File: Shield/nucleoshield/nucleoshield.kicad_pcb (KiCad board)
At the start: 2 copper layers, 99.6 x 99.6 mm, 2 parts, among them J1 Conn_02x19_Odd_Even, J2 Conn_02x19_Odd_Even

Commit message: Schematic and pcb ready
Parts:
- added C1: 470u, Capacitor_THT:CP_Radial_D8.0mm_P3.50mm, F.Cu at (98.3, 121.7)
- added C2: 47u, Capacitor_SMD:C_1206_3216Metric, F.Cu at (74.5, 126.7)
- added C3: 100n, Capacitor_SMD:C_1206_3216Metric, F.Cu at (95.6, 97.6)
- added C4: 100n, Capacitor_SMD:C_1206_3216Metric, F.Cu at (100.0, 114.4)
- added C5: 470u, Capacitor_THT:CP_Radial_D8.0mm_P3.50mm, F.Cu at (86.4, 95.8)
- added C6: 10u, Capacitor_SMD:C_1206_3216Metric, F.Cu at (102.9, 56.5)
- added C7: 100n, Capacitor_SMD:C_1206_3216Metric, F.Cu at (116.0, 46.5)
- added D1: LED, LED_SMD:LED_0805_2012Metric, F.Cu at (75.4, 62.8)
- added IC1: L80-M39, componentLib:L80-M39, F.Cu at (81.7, 51.4)
- added J10: ENCODER_3, Connector_PinSocket_2.54mm:PinSocket_1x04_P2.54mm_Vertical, F.Cu at (147.4, 107.7)
- added J11: MPU9250, Connector_PinHeader_2.54mm:PinHeader_1x10_P2.54mm_Vertical, F.Cu at (109.2, 45.1)
- added J3: POWER, Connector_PinHeader_2.54mm:PinHeader_1x03_P2.54mm_Vertical, F.Cu at (86.7, 130.7)
- added J4: MOTOR_1, Connector_PinSocket_2.54mm:PinSocket_1x04_P2.54mm_Vertical, F.Cu at (60.6, 94.2)
- added J5: ENCODER_1, Connector_PinSocket_2.54mm:PinSocket_1x04_P2.54mm_Vertical, F.Cu at (60.6, 107.7)
- added J6: ENCODER_2, Connector_PinSocket_2.54mm:PinSocket_1x04_P2.54mm_Vertical, F.Cu at (113.5, 130.6)
- added J7: MOTOR_2, Connector_PinSocket_2.54mm:PinSocket_1x04_P2.54mm_Vertical, F.Cu at (98.8, 130.6)
- added J8: LCD_I2C, Connector_PinSocket_2.54mm:PinSocket_1x04_P2.54mm_Vertical, F.Cu at (146.7, 53.4)
- added J9: MOTOR_3, Connector_PinSocket_2.54mm:PinSocket_1x04_P2.54mm_Vertical, F.Cu at (147.4, 94.2)
- added JP1: AVDD-3.3V, Jumper:SolderJumper-2_P1.3mm_Bridged2Bar_Pad1.0x1.5mm, F.Cu at (146.9, 82.7)
- added Q1: BSS138, Package_TO_SOT_SMD:SOT-23, F.Cu at (136.4, 55.3)
- added Q2: BSS138, Package_TO_SOT_SMD:SOT-23, F.Cu at (136.4, 61.2)
- added R1: 10k, Resistor_SMD:R_0805_2012Metric, F.Cu at (79.2, 119.6)
- added R2: 2k, Resistor_SMD:R_0805_2012Metric, F.Cu at (79.2, 127.0)
- added R3: 2K, Resistor_SMD:R_0805_2012Metric, F.Cu at (131.0, 55.3)
- added R4: 2K, Resistor_SMD:R_0805_2012Metric, F.Cu at (130.9, 61.2)
- added R5: 2K, Resistor_SMD:R_0805_2012Metric, F.Cu at (141.6, 53.9)
- added R6: 2K, Resistor_SMD:R_0805_2012Metric, F.Cu at (143.0, 61.1)
- added R7: 1K, Resistor_SMD:R_0805_2012Metric, F.Cu at (70.9, 61.9)
- added TP1: AVDD, TestPoint:TestPoint_THTPad_1.0x1.0mm_Drill0.5mm, F.Cu at (146.2, 78.1)
- moved J2 33.2 mm to (133.0, 74.8)
- moved J1 33.1 mm to (72.0, 74.8)
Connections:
- J1 pad 1: unconnected-(J1-Pad1) -> GPS_UART_RX
- J1 pad 12: unconnected-(J1-Pad12) -> IOREF
- J1 pad 14: unconnected-(J1-Pad14) -> RESET
- J1 pad 16: unconnected-(J1-Pad16) -> ENCODER_VCC
- J1 pad 18: unconnected-(J1-Pad18) -> LOGIC_5V
- J1 pad 19: unconnected-(J1-Pad19) -> ENCODER_GND
- J1 pad 2: unconnected-(J1-Pad2) -> GPS_UART_TX
- J1 pad 20: unconnected-(J1-Pad20) -> ENCODER_GND
- J1 pad 22: unconnected-(J1-Pad22) -> ENCODER_GND
- J1 pad 23: unconnected-(J1-Pad23) -> ENCODER_A1
- J1 pad 24: unconnected-(J1-Pad24) -> VIN
- J1 pad 25: unconnected-(J1-Pad25) -> ENCODER_B1
- J1 pad 27: unconnected-(J1-Pad27) -> ENCODER_A2
- J1 pad 29: unconnected-(J1-Pad29) -> ENCODER_B2
- J1 pad 3: unconnected-(J1-Pad3) -> GPS_RESET
- J1 pad 31: unconnected-(J1-Pad31) -> ENCODER_A3
- J1 pad 33: unconnected-(J1-Pad33) -> VBAT
- J1 pad 35: unconnected-(J1-Pad35) -> ENCODER_B3
- J1 pad 38: unconnected-(J1-Pad38) -> BAT_ADC
- J1 pad 5: unconnected-(J1-Pad5) -> VDD
- J1 pad 6: unconnected-(J1-Pad6) -> E5V
- J1 pad 8: unconnected-(J1-Pad8) -> ENCODER_GND
- J2 pad 17: unconnected-(J2-Pad17) -> SCL
- J2 pad 19: unconnected-(J2-Pad19) -> SDA
- J2 pad 20: unconnected-(J2-Pad20) -> ENCODER_GND
- J2 pad 21: unconnected-(J2-Pad21) -> INB1
- J2 pad 23: unconnected-(J2-Pad23) -> INA1
- J2 pad 25: unconnected-(J2-Pad25) -> SCL2
- J2 pad 29: unconnected-(J2-Pad29) -> INB3
- J2 pad 3: unconnected-(J2-Pad3) -> INA2
- J2 pad 31: unconnected-(J2-Pad31) -> SDA2
- J2 pad 4: unconnected-(J2-Pad4) -> INA3
- J2 pad 5: unconnected-(J2-Pad5) -> INB2
- J2 pad 7: unconnected-(J2-Pad7) -> AVDD
- J2 pad 8: unconnected-(J2-Pad8) -> U5V
- J2 pad 9: unconnected-(J2-Pad9) -> ENCODER_GND
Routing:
- net ENCODER_VCC: track 0.00 -> 363.9 mm
- net LOGIC_5V: track 0.00 -> 95.7 mm
- net ENCODER_A3: track 0.00 -> 85.7 mm, vias 0 -> 2
- net ENCODER_B3: track 0.00 -> 84.7 mm, vias 0 -> 2
- net ENCODER_B2: track 0.00 -> 80.4 mm, vias 0 -> 1
- net ENCODER_A2: track 0.00 -> 76.7 mm
- net INA1: track 0.00 -> 75.2 mm, vias 0 -> 2
- net INB1: track 0.00 -> 73.0 mm, vias 0 -> 2
- net INA2: track 0.00 -> 69.2 mm
- net INB2: track 0.00 -> 66.1 mm
- net SDA2: track 0.00 -> 66.1 mm, vias 0 -> 3
- net SCL: track 0.00 -> 64.1 mm
- net SDA: track 0.00 -> 63.6 mm
- net E5V: track 0.00 -> 63.0 mm
- net SCL2: track 0.00 -> 49.9 mm, vias 0 -> 2
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- added copper zone on B.Cu, net ENCODER_GND
- added copper zone on F.Cu, net ENCODER_GND
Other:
- board text added: "3V3"
- board text added: "5V"
- board text added: "AD0"
- board text added: "BAT"
- board text added: "ECL"
- board text added: "EDA"
- board text added: "ENA"
- board text added: "ENB"
- board text added: "FSYNC"
- board text added: "GND"
- board text added: "INA"
- board text added: "INB"
- board text added: "INT"
- board text added: "NCS"
- board text added: "SCL"
- board text added: "SDA"

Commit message: power modifications
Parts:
- added JP2: Jumper_3_Open, Connector_PinSocket_2.54mm:PinSocket_1x03_P2.54mm_Vertical, F.Cu at (82.8, 89.1)
- J10, J4, J5, J6, J7, J8, J9: footprint Connector_PinSocket_2.54mm:PinSocket_1x04_P2.54mm_Vertical -> Connector_JST:JST_EH_B4B-EH-A_1x04_P2.50mm_Vertical
- moved R6 1.79 mm to (141.2, 61.2), turned to 180 degrees
- moved J10 0.30 mm to (147.4, 108.0), turned to -90 degrees
- moved J9 0.15 mm to (147.4, 94.3), turned to -90 degrees
- turned J4 to -90 degrees
- turned J5 to -90 degrees
- turned J6 to 0 degrees
- turned J7 to 0 degrees
- turned J8 to -90 degrees
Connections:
- J1 pad 18: LOGIC_5V -> NUCLEO_5V
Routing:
- net NUCLEO_5V: track 0.00 -> 10.8 mm
- net E5V: track 63.0 -> 67.3 mm
- net Net-(J8-Pad4): track 12.3 -> 10.6 mm
- net LOGIC_5V: track 95.7 -> 95.0 mm
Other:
- board text added: "DCDC_5V"
- board text added: "NUC_5V"

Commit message: Power connector
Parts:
- added J12: Screw_Terminal_01x02, TerminalBlock:TerminalBlock_Altech_AK300-2_P5.00mm, F.Cu at (71.9, 43.7)
- added J13: Screw_Terminal_01x02, TerminalBlock:TerminalBlock_Altech_AK300-2_P5.00mm, F.Cu at (58.2, 43.2)
- added JP3: Jumper_3_Open, Connector_PinSocket_2.54mm:PinSocket_1x03_P2.54mm_Vertical, F.Cu at (79.7, 89.9)
- moved JP1 25.5 mm to (121.9, 87.9), turned to -90 degrees
- moved TP1 20.8 mm to (126.0, 82.8)
- moved JP2 12.2 mm to (95.0, 88.9)
- moved C5 7.58 mm to (94.0, 95.9)
- moved C3 4.98 mm to (100.6, 97.6)
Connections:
- net E5V renamed 5V_DCDC
- J1 pad 16: ENCODER_VCC -> NUCLEO_3V3
- JP1 pad 2: ENCODER_VCC -> NUCLEO_3V3
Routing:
- net NUCLEO_3V3: track 0.00 -> 83.5 mm, vias 0 -> 2
- net 5V_DCDC: track 67.3 -> 135.7 mm
- net 3V3_DCDC: track 0.00 -> 48.5 mm
- net ENCODER_VCC: track 363.9 -> 348.8 mm
- net NUCLEO_5V: track 10.8 -> 23.1 mm, vias 0 -> 1
- net LOGIC_5V: track 95.0 -> 84.5 mm
- net AVDD: track 19.0 -> 13.3 mm

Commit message: small changes
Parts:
- JP2, JP3: footprint Connector_PinSocket_2.54mm:PinSocket_1x03_P2.54mm_Vertical -> Connector_PinHeader_2.54mm:PinHeader_1x03_P2.54mm_Vertical
- moved D1 29.2 mm to (94.5, 40.6), turned to -90 degrees
- moved R7 29.2 mm to (94.5, 44.7), turned to -90 degrees
- moved C7 18.8 mm to (100.1, 56.4)
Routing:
- net Net-(IC1-Pad6): track 36.4 -> 5.67 mm
- net Net-(D1-Pad2): track 3.57 -> 2.21 mm

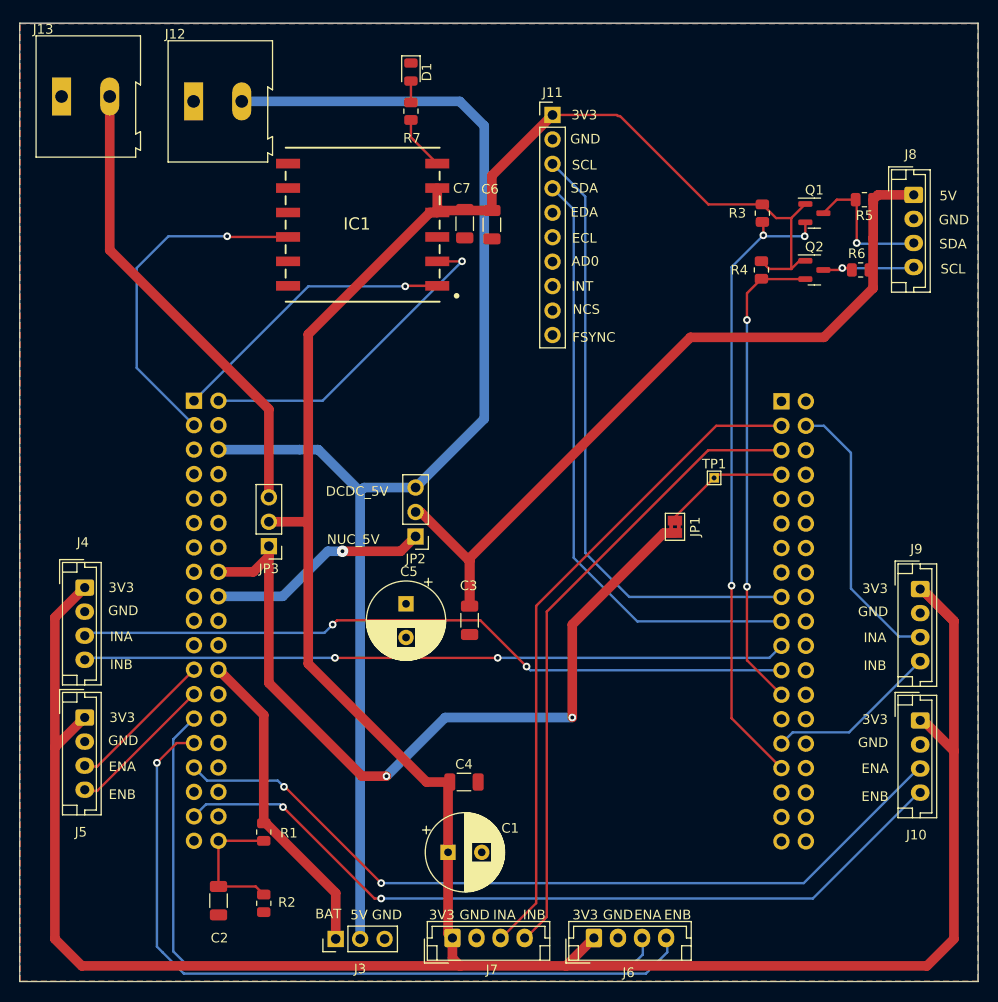
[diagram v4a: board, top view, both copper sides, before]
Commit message: Csatlakozók megváltoztatva, polaritásvédelem, apróbb javítások
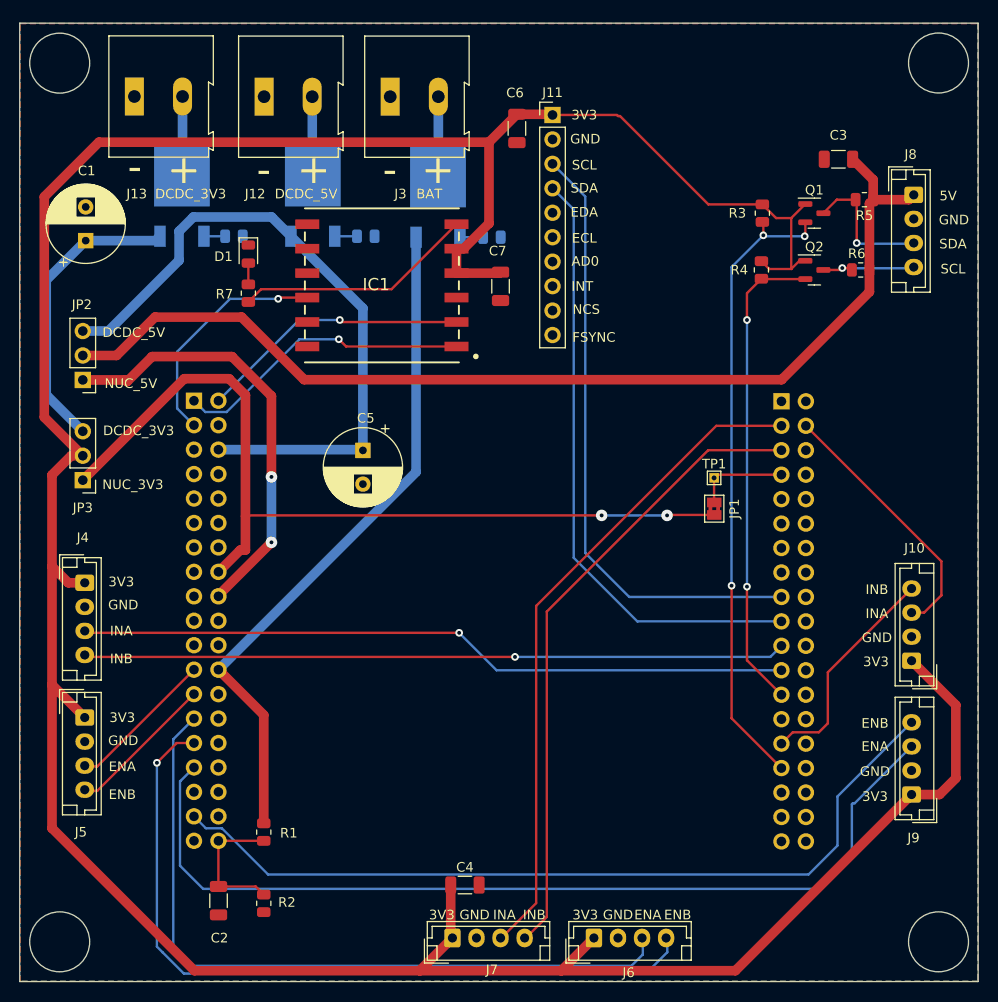
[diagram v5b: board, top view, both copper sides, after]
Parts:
- added Q3: AOD409, Package_TO_SOT_SMD:TO-252-2, B.Cu at (84.3, 53.5)
- added Q4: AOD409, Package_TO_SOT_SMD:TO-252-2, B.Cu at (70.7, 53.5)
- added Q5: AOD409, Package_TO_SOT_SMD:TO-252-2, B.Cu at (97.3, 53.6)
- added R10: 10k, Resistor_SMD:R_0805_2012Metric, B.Cu at (102.9, 57.8)
- added R8: 10k, Resistor_SMD:R_0805_2012Metric, B.Cu at (89.8, 57.7)
- added R9: 10k, Resistor_SMD:R_0805_2012Metric, B.Cu at (76.1, 57.7)
- C2: value 47u -> 22u
- J12: value Screw_Terminal_01x02 -> 5V_DCDC
- J13: value Screw_Terminal_01x02 -> 3V3_DCDC
- J3: value POWER -> Battery; footprint Connector_PinHeader_2.54mm:PinHeader_1x03_P2.54mm_Vertical -> TerminalBlock:TerminalBlock_Altech_AK300-2_P5.00mm
- moved J3 87.7 mm to (92.3, 43.2), turned to 0 degrees
- moved C1 73.9 mm to (60.7, 58.2), turned to 90 degrees
- moved C3 61.3 mm to (138.9, 49.7), turned to 180 degrees
- moved JP2 38.2 mm to (60.4, 72.6)
- moved D1 25.4 mm to (77.6, 59.5)
- moved R7 25.4 mm to (77.6, 63.6)
- moved JP3 20.5 mm to (60.4, 83.0)
- moved C5 16.6 mm to (89.5, 79.9)
- moved C4 10.7 mm to (100.1, 125.1)
- moved C6 10.3 mm to (105.5, 46.5)
- moved J10 7.75 mm to (146.5, 115.7), turned to 90 degrees
- moved J13 7.57 mm to (65.8, 43.2)
- moved J9 7.50 mm to (146.5, 101.8), turned to 90 degrees
- moved C7 7.50 mm to (103.8, 62.9)
- moved J12 7.34 mm to (79.2, 43.2)
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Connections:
- C1 pad 1: ENCODER_VCC -> 3V3_DCDC
- C5 pad 1: LOGIC_5V -> 5V_DCDC
- J12 pad 2: 5V_DCDC -> Net-(J12-Pad2)
- J13 pad 2: 3V3_DCDC -> Net-(J13-Pad2)
- J3 pad 1: VIN -> ENCODER_GND
- J3 pad 2: 5V_DCDC -> Net-(J3-Pad2)
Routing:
- net 5V_DCDC: track 135.7 -> 69.5 mm
- net VIN: track 33.2 -> 71.3 mm
- net LOGIC_5V: track 84.5 -> 109.1 mm
- net NUCLEO_5V: track 23.1 -> 45.5 mm, vias 1 -> 2
- net Net-(IC1-Pad6): track 5.67 -> 25.0 mm
- net 3V3_DCDC: track 48.5 -> 31.0 mm
- net ENCODER_VCC: track 348.9 -> 334.0 mm
- net GPS_RESET: track 35.9 -> 24.2 mm
- net ENCODER_A3: track 85.7 -> 96.8 mm, vias 2 -> 0
- net Net-(J3-Pad2): track 0.00 -> 8.31 mm
- net Net-(J13-Pad2): track 0.00 -> 8.24 mm
- net Net-(J12-Pad2): track 0.00 -> 8.23 mm
- net NUCLEO_3V3: track 83.5 -> 90.6 mm
- net GPS_UART_TX: track 33.9 -> 28.3 mm
- net INB3: track 18.0 -> 23.3 mm
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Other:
- outline, holes or cut-outs redrawn
- board text added: "+"
- board text added: "-"
- board text added: "DCDC_3V3"
- board text added: "NUC_3V3"

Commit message: Fetek kicserélve
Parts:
- Q3, Q4, Q5: value AOD409 -> AO3401A; footprint Package_TO_SOT_SMD:TO-252-2 -> Package_TO_SOT_SMD:SOT-23
- moved R8 4.04 mm to (89.2, 53.7)
- moved R10 3.98 mm to (102.1, 53.9)
- moved R9 2.73 mm to (75.0, 55.2)
- moved Q3 0.81 mm to (84.2, 52.7)
- moved Q4 0.80 mm to (70.7, 52.7)
- moved Q5 0.50 mm to (97.3, 53.1)
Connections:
- Q3 pad 2: Net-(J12-Pad2) -> 5V_DCDC
- Q3 pad 3: 5V_DCDC -> Net-(J12-Pad2)
- Q4 pad 2: Net-(J13-Pad2) -> 3V3_DCDC
- Q4 pad 3: 3V3_DCDC -> Net-(J13-Pad2)
- Q5 pad 2: Net-(J3-Pad2) -> VIN
- Q5 pad 3: VIN -> Net-(J3-Pad2)
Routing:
- net 3V3_DCDC: track 31.0 -> 35.6 mm
- net VIN: track 71.3 -> 75.7 mm
- net 5V_DCDC: track 69.5 -> 71.2 mm
- net Net-(R9-Pad1): track 2.21 -> 3.08 mm
- net Net-(R8-Pad1): track 2.31 -> 3.16 mm
- net Net-(R10-Pad1): track 2.41 -> 2.99 mm

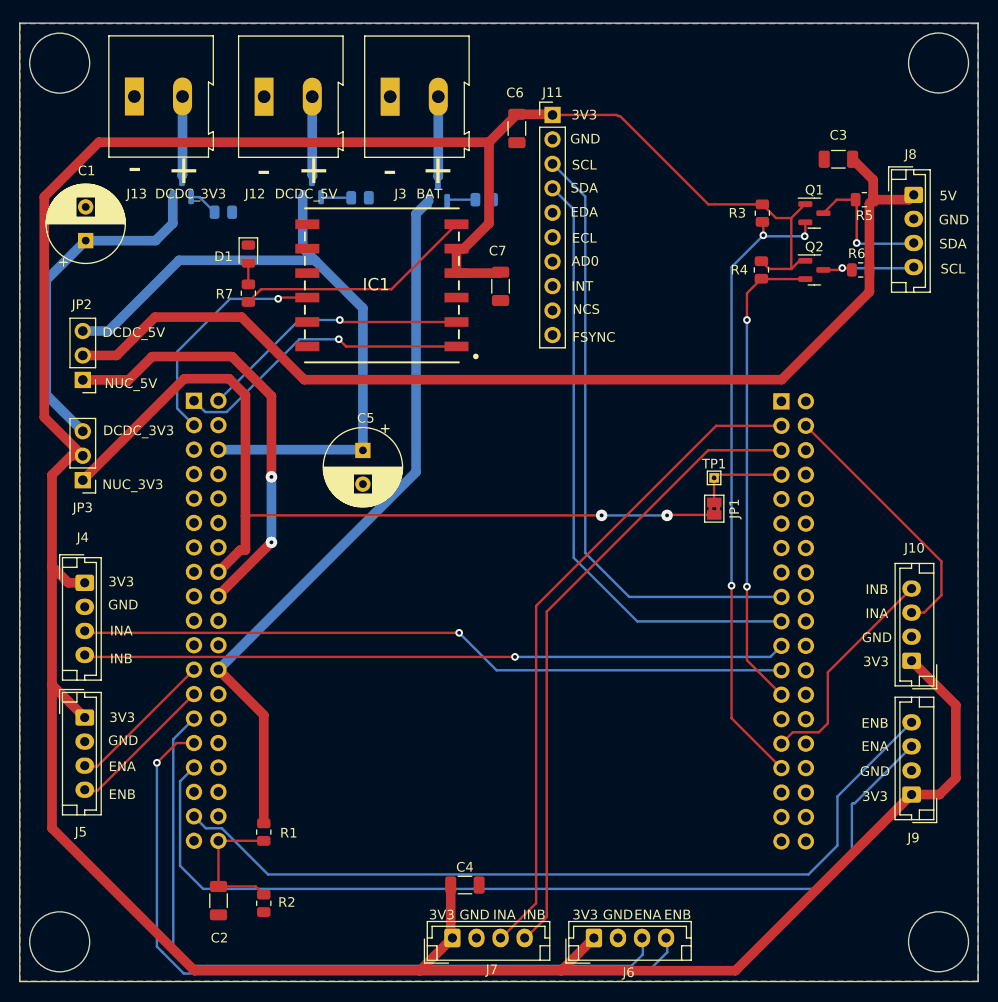
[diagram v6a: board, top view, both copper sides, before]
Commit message: Enkóderek timer bemenetekhez rendelve
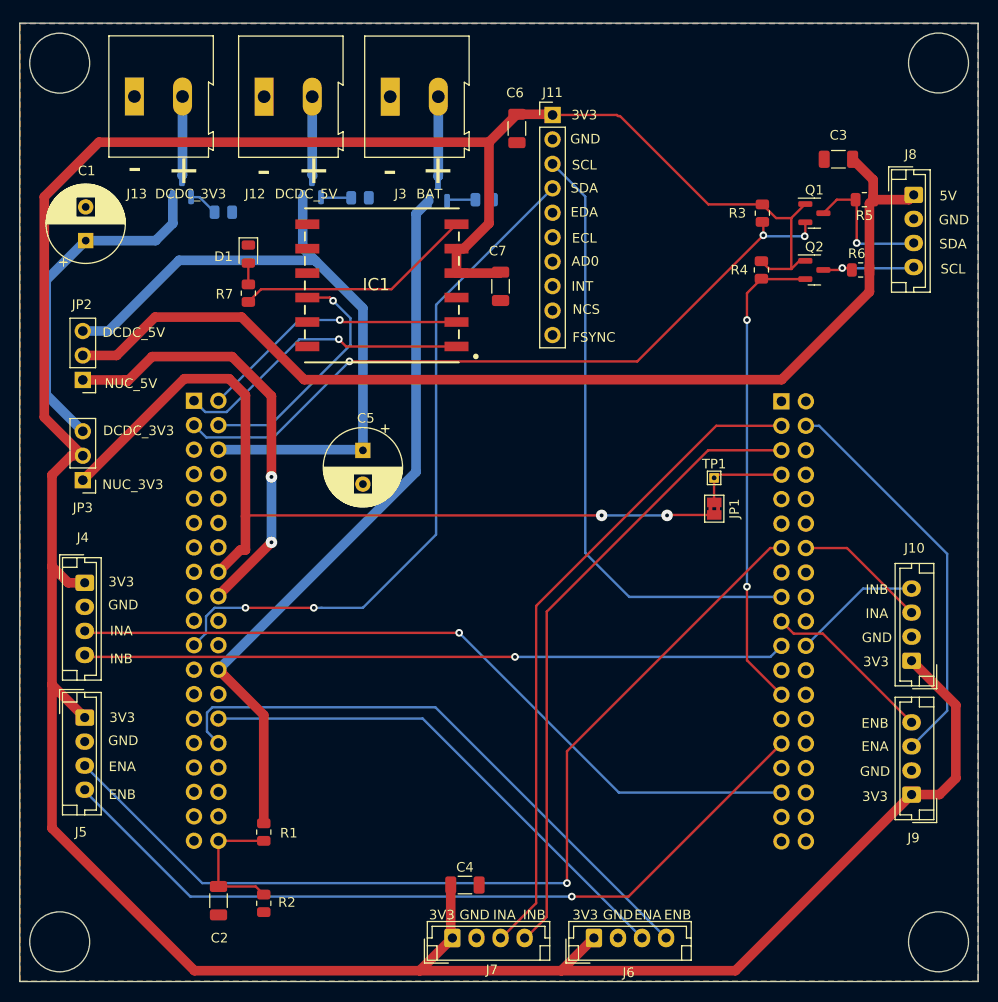
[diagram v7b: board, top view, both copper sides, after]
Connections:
- J1 pad 21: unconnected-(J1-Pad21) -> SDA
- J1 pad 23: ENCODER_A1 -> unconnected-(J1-Pad23)
- J1 pad 25: ENCODER_B1 -> unconnected-(J1-Pad25)
- J1 pad 27: ENCODER_A2 -> unconnected-(J1-Pad27)
- J1 pad 28: unconnected-(J1-Pad28) -> ENCODER_A2
- J1 pad 29: ENCODER_B2 -> unconnected-(J1-Pad29)
- J1 pad 3: GPS_RESET -> SDA2
- J1 pad 30: unconnected-(J1-Pad30) -> ENCODER_B2
- J1 pad 31: ENCODER_A3 -> unconnected-(J1-Pad31)
- J1 pad 35: ENCODER_B3 -> unconnected-(J1-Pad35)
- J1 pad 4: unconnected-(J1-Pad4) -> GPS_RESET
- J2 pad 13: unconnected-(J2-Pad13) -> ENCODER_A1
- J2 pad 14: unconnected-(J2-Pad14) -> INA3
- J2 pad 19: SDA -> ENCODER_B3
- J2 pad 22: unconnected-(J2-Pad22) -> INB3
- J2 pad 23: INA1 -> unconnected-(J2-Pad23)
- J2 pad 29: INB3 -> ENCODER_B1
- J2 pad 31: SDA2 -> unconnected-(J2-Pad31)
- J2 pad 33: unconnected-(J2-Pad33) -> INA1
- J2 pad 4: INA3 -> ENCODER_A3
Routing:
- net ENCODER_A1: track 15.5 -> 99.9 mm, vias 0 -> 1
- net ENCODER_B3: track 86.6 -> 17.9 mm
- net ENCODER_B1: track 15.5 -> 83.6 mm, vias 0 -> 1
- net ENCODER_A3: track 96.8 -> 41.7 mm
- net ENCODER_A2: track 76.7 -> 53.5 mm
- net ENCODER_B2: track 80.4 -> 61.5 mm, vias 1 -> 0
- net INA3: track 27.3 -> 13.8 mm
- net INB3: track 23.3 -> 13.4 mm
- net SDA2: track 66.1 -> 75.6 mm
- net SDA: track 63.6 -> 71.9 mm, vias 0 -> 2
- net INA1: track 74.1 -> 79.3 mm
- net GPS_RESET: track 24.2 -> 25.3 mm
